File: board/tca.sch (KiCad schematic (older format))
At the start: 23 parts, among them IC1 ATMEGA328-A, P1 CONN_2, P2 CONN_3X2, P3 CONN_8X2, P4 CONN_8X2, P5 CONN_8X2, P6 CONN_8X2, P7 CONN_8X2, P8 CONN_8X2, U1 TLC5941, U2 TLC5941, U3 TLC5941, Y1 RESONATEUR

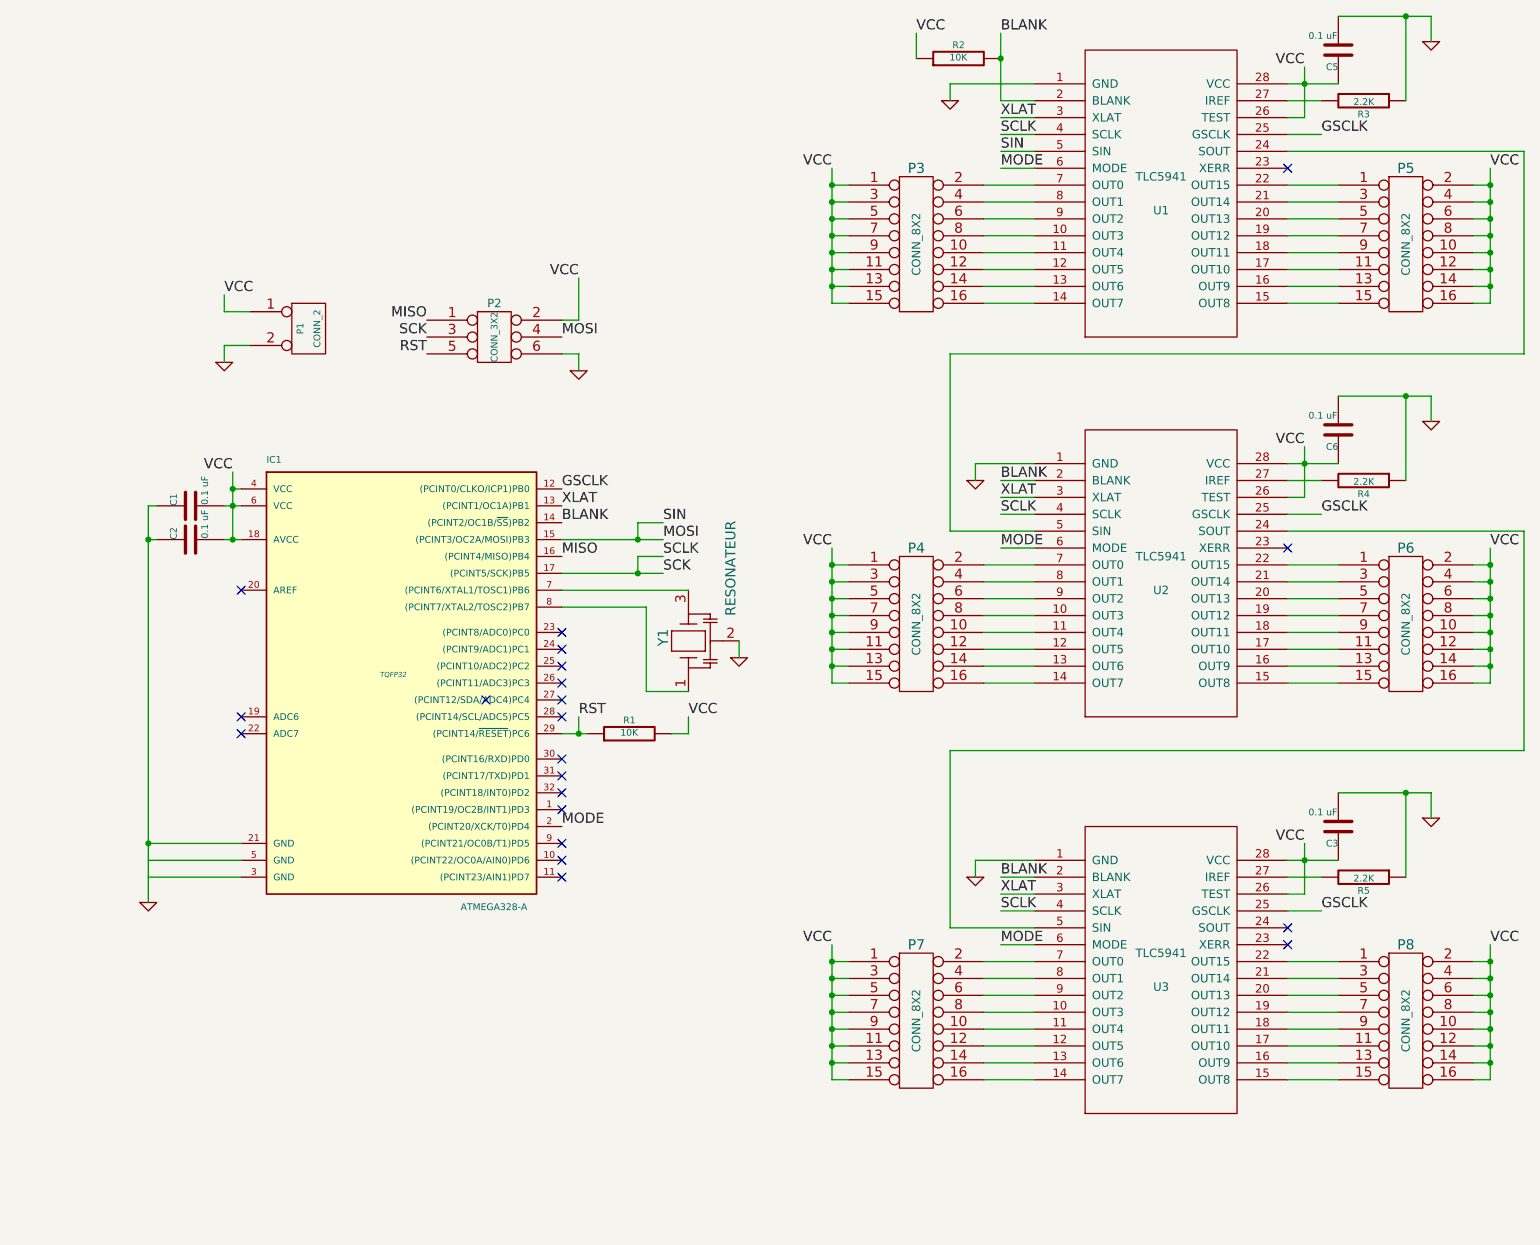
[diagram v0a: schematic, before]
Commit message: Modified board to include SD card and other improvements.
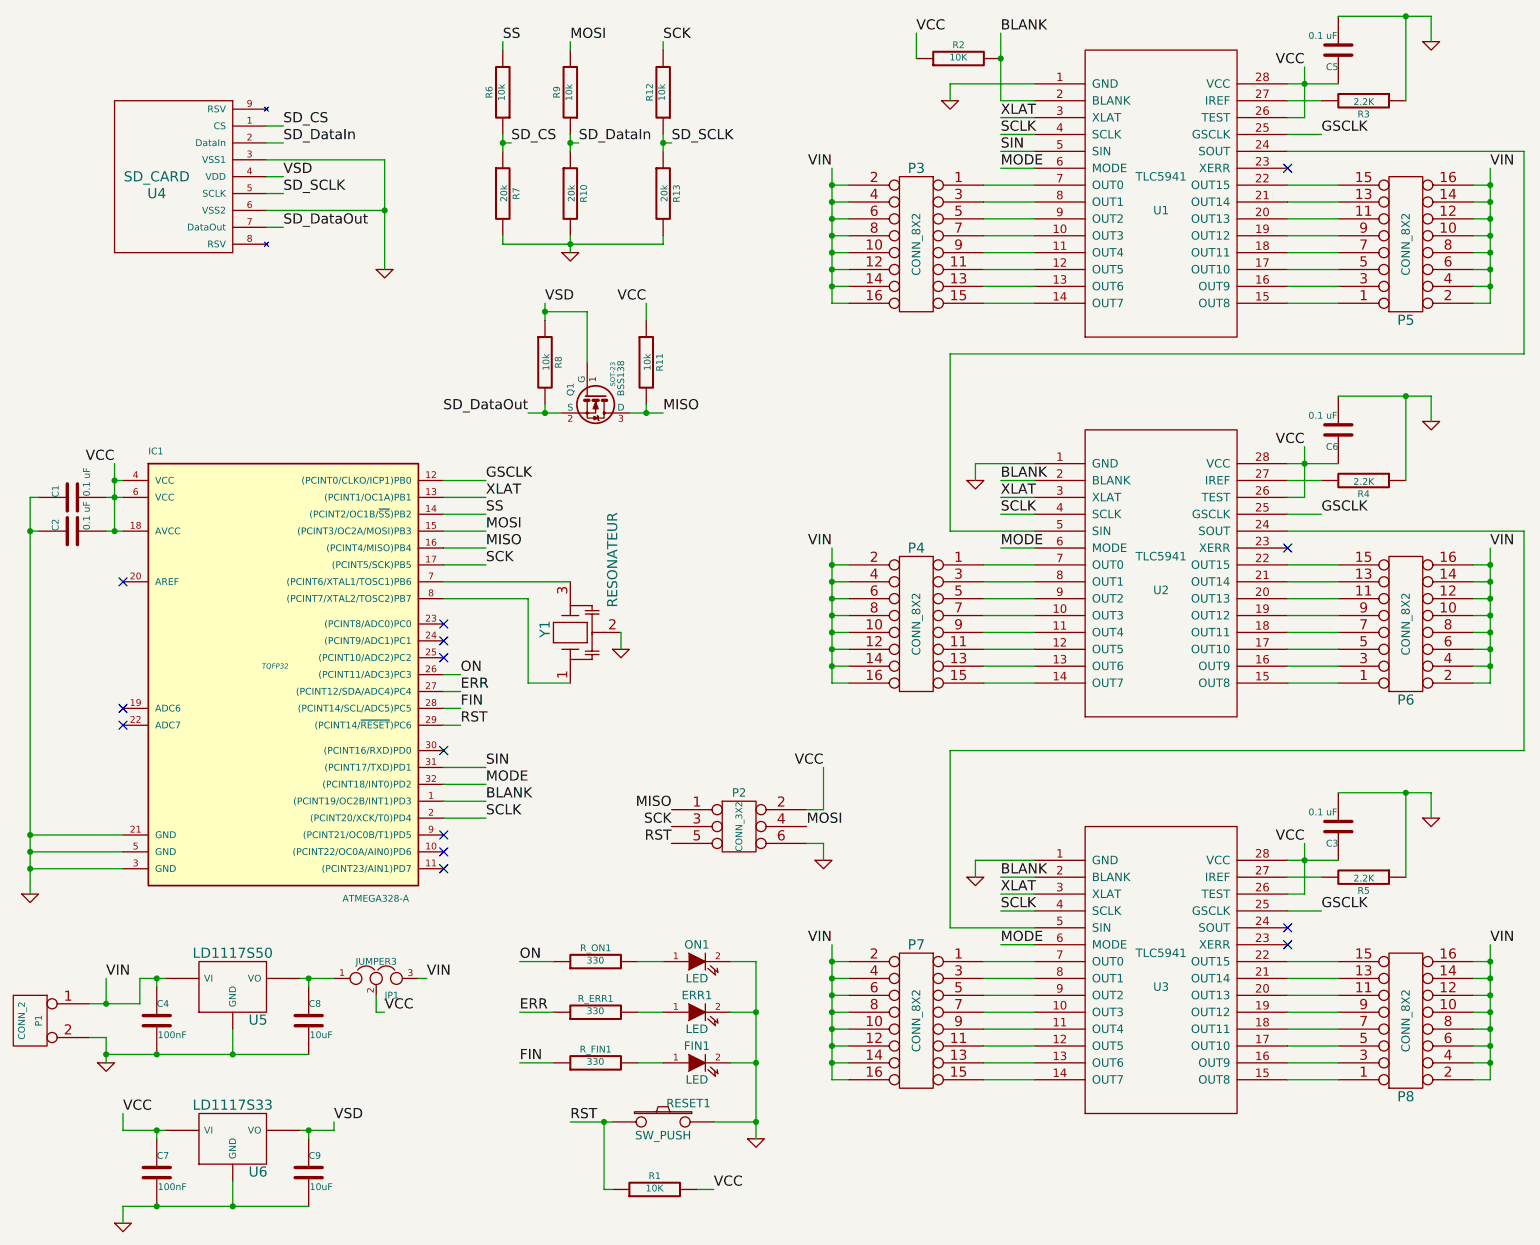
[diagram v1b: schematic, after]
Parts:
- added C4, C7: 100nF, ~, symbol C
- added C8, C9: 10uF, ~, symbol C
- added ERR1, FIN1, ON1: LED, ~, symbol LED
- added JP1: JUMPER3, ~, symbol JUMPER3
- added Q1: BSS138, SOT-23, symbol BSS138
- added R10, R13, R7: 20k, ~, symbol R
- added R11, R12, R6, R8, R9: 10k, ~, symbol R
- added RESET1: SW_PUSH, ~, symbol SW_PUSH
- added R_ERR1, R_FIN1, R_ON1: 330, ~, symbol R
- added U4: SD_CARD, symbol SD_CARD
- added U5: LD1117S50, ~, symbol LD1117S50
- added U6: LD1117S33, ~, symbol LD1117S33
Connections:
- net BLANK: now also IC1.1 ((PCINT19/OC2B/INT1)PD3); no longer IC1.14 ((PCINT2/OC1B/~SS~)PB2)
- net GND: now also IC1.3 (GND), IC1.5 (GND), C4.2, C7.2, C8.2, C9.2, ERR1.2 (K), FIN1.2 (K), ON1.2 (K), R10.2, R13.2, R7.2, RESET1.2, U4.3 (VSS1), U4.6 (VSS2), U5.1 (GND), U6.1 (GND)
- net MISO: now also Q1.3 (D), R11.2
- net MODE: now also IC1.32 ((PCINT18/INT0)PD2); no longer IC1.2 ((PCINT20/XCK/T0)PD4)
- net MOSI: now also R9.2; no longer U1.5 (SIN)
- net RST: now also RESET1.1
- net SCK: now also R12.2; no longer U1.4 (SCLK), U2.4 (SCLK), U3.4 (SCLK)
- net VCC: now also C7.1, JP1.2, R11.1, U6.3 (VI); no longer P1.1 (P1), P3.1, P3.11, P3.13, P3.15, P3.3, P3.5, P3.7, P3.9, P4.1, P4.11, P4.13, P4.15, P4.3, P4.5, P4.7, P4.9, P5.10, P5.12, P5.14, P5.16, P5.2, P5.4, P5.6, P5.8, P6.10, P6.12, P6.14, P6.16, P6.2, P6.4, P6.6, P6.8, P7.1, P7.11, P7.13, P7.15, P7.3, P7.5, P7.7, P7.9, P8.10, P8.12, P8.14, P8.16, P8.2, P8.4, P8.6, P8.8
- net at U1.10 (OUT3): now also P3.7; no longer P3.8
- net at U1.11 (OUT4): now also P3.9; no longer P3.10
- net at U1.12 (OUT5): now also P3.11; no longer P3.12
- net at U1.13 (OUT6): now also P3.13; no longer P3.14
- net at U1.14 (OUT7): now also P3.15; no longer P3.16
- net at U1.15 (OUT8): now also P5.1; no longer P5.15
- net at U1.16 (OUT9): now also P5.3; no longer P5.13
- net at U1.17 (OUT10): now also P5.5; no longer P5.11
- net at U1.18 (OUT11): now also P5.7; no longer P5.9
- net at U1.19 (OUT12): now also P5.9; no longer P5.7
- net at U1.20 (OUT13): now also P5.11; no longer P5.5
- net at U1.21 (OUT14): now also P5.13; no longer P5.3
- net at U1.22 (OUT15): now also P5.15; no longer P5.1
- net at U1.7 (OUT0): now also P3.1; no longer P3.2
- net at U1.8 (OUT1): now also P3.3; no longer P3.4
- net at U1.9 (OUT2): now also P3.5; no longer P3.6
- net at U2.10 (OUT3): now also P4.7; no longer P4.8
- net at U2.11 (OUT4): now also P4.9; no longer P4.10
- net at U2.12 (OUT5): now also P4.11; no longer P4.12
- net at U2.13 (OUT6): now also P4.13; no longer P4.14
- net at U2.14 (OUT7): now also P4.15; no longer P4.16
- net at U2.15 (OUT8): now also P6.1; no longer P6.15
- net at U2.16 (OUT9): now also P6.3; no longer P6.13
- net at U2.17 (OUT10): now also P6.5; no longer P6.11
- net at U2.18 (OUT11): now also P6.7; no longer P6.9
- net at U2.19 (OUT12): now also P6.9; no longer P6.7
- net at U2.20 (OUT13): now also P6.11; no longer P6.5
- net at U2.21 (OUT14): now also P6.13; no longer P6.3
- net at U2.22 (OUT15): now also P6.15; no longer P6.1
- net at U2.7 (OUT0): now also P4.1; no longer P4.2
- net at U2.8 (OUT1): now also P4.3; no longer P4.4
- net at U2.9 (OUT2): now also P4.5; no longer P4.6
- net ON: now reaches IC1.26 ((PCINT11/ADC3)PC3)
- net ON: now also R_ON1.1
- net ERR: now reaches IC1.27 ((PCINT12/SDA/ADC4)PC4)
- net ERR: now also R_ERR1.1
- net FIN: now reaches IC1.28 ((PCINT14/SCL/ADC5)PC5)
- net FIN: now also R_FIN1.1
- net SIN: now reaches IC1.31 ((PCINT17/TXD)PD1)
- net SIN: now also U1.5 (SIN)
- net at U3.10 (OUT3): now also P7.7; no longer P7.8
- net at U3.11 (OUT4): now also P7.9; no longer P7.10
- net at U3.12 (OUT5): now also P7.11; no longer P7.12
- net at U3.13 (OUT6): now also P7.13; no longer P7.14
- net at U3.14 (OUT7): now also P7.15; no longer P7.16
- net at U3.15 (OUT8): now also P8.1; no longer P8.15
- net at U3.16 (OUT9): now also P8.3; no longer P8.13
- net at U3.17 (OUT10): now also P8.5; no longer P8.11
- net at U3.18 (OUT11): now also P8.7; no longer P8.9
- net at U3.19 (OUT12): now also P8.9; no longer P8.7
- net at U3.20 (OUT13): now also P8.11; no longer P8.5
- net at U3.21 (OUT14): now also P8.13; no longer P8.3
- net at U3.22 (OUT15): now also P8.15; no longer P8.1
- net at U3.7 (OUT0): now also P7.1; no longer P7.2
- net at U3.8 (OUT1): now also P7.3; no longer P7.4
- net at U3.9 (OUT2): now also P7.5; no longer P7.6
- new net: ON1.1 (A), R_ON1.2
- new net: ERR1.1 (A), R_ERR1.2
- new net: FIN1.1 (A), R_FIN1.2
- new net: C8.1, JP1.1, U5.2 (VO)
- new net SCLK: IC1.2 ((PCINT20/XCK/T0)PD4), U1.4 (SCLK), U2.4 (SCLK), U3.4 (SCLK)
- new net SD_CS: R6.1, R7.1, U4.1 (CS)
- new net SD_DataIn: R10.1, R9.1, U4.2 (DataIn)
- new net SD_DataOut: Q1.2 (S), R8.2, U4.7 (DataOut)
- new net SD_SCLK: R12.1, R13.1, U4.5 (SCLK)
- new net SS: IC1.14 ((PCINT2/OC1B/~SS~)PB2), R6.2
- new net VIN: C4.1, JP1.3, P1.1 (P1), P3.10, P3.12, P3.14, P3.16, P3.2, P3.4, P3.6, P3.8, P4.10, P4.12, P4.14, P4.16, P4.2, P4.4, P4.6, P4.8, P5.10, P5.12, P5.14, P5.16, P5.2, P5.4, P5.6, P5.8, P6.10, P6.12, P6.14, P6.16, P6.2, P6.4, P6.6, P6.8, P7.10, P7.12, P7.14, P7.16, P7.2, P7.4, P7.6, P7.8, P8.10, P8.12, P8.14, P8.16, P8.2, P8.4, P8.6, P8.8, U5.3 (VI)
- new net VSD: C9.1, Q1.1 (G), R8.1, U4.4 (VDD), U6.2 (VO)
- no-connect marks 21 -> 14
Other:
- moved on the sheet: C1, C2, IC1, P1, P2, R1, Y1
